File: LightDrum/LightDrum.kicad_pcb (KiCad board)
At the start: 4 copper layers, 108 x 83 mm, 221 parts, among them J102 JTAG, J1201 0525593652, J1203 PWR-CONN, J201 XLR3, J202 SJ-43515RS-SMT-TR, J601 LED D-SUB, J901 STD BARREL JACK, J902 STD BARREL JACK, K901 ALQ112, K902 ALQ112, Q101 RQ5A030AP, SW101 BOOT1, SW102 BOOT0, T701 NET-TIE, T702 NET-TIE, T703 NET-TIE, T704 NET-TIE, T705 NET-TIE, T706 NET-TIE, T707 NET-TIE, T708 NET-TIE, T709 NET-TIE, T710 NET-TIE, T711 NET-TIE, T712 NET-TIE, T713 NET-TIE, T714 NET-TIE, T715 NET-TIE, T716 NET-TIE, U1001 AP3401, U1002 LM22673-SOIC, U101 TCAN1044, U102 24LC04, U301 PCA9634_TSSOP20, U302 SQ2310ES_SOT23, U303 SQ2310ES_SOT23, U304 SQ2310ES_SOT23, U305 SQ2310ES_SOT23, U306 SQ2310ES_SOT23, U307 SQ2310ES_SOT23, U308 SQ2310ES_SOT23, U309 SQ2310ES_SOT23, U401 PCA9634_TSSOP20, U402 SQ2310ES_SOT23, U403 SQ2310ES_SOT23, U404 SQ2310ES_SOT23, U405 SQ2310ES_SOT23, U406 SQ2310ES_SOT23, U407 SQ2310ES_SOT23, U408 SQ2310ES_SOT23, U409 SQ2310ES_SOT23, U501 PCA9634_TSSOP20, U502 SQ2310ES_SOT23, U503 SQ2310ES_SOT23, U504 SQ2310ES_SOT23, U505 SQ2310ES_SOT23, U506 SQ2310ES_SOT23, U507 SQ2310ES_SOT23, U508 SQ2310ES_SOT23, U509 SQ2310ES_SOT23, U701 INA4181 A2, U702 INA4181 A2, U901 74HC2G08, U902 SSM3K361R_SOT23F, Y101 8MHz

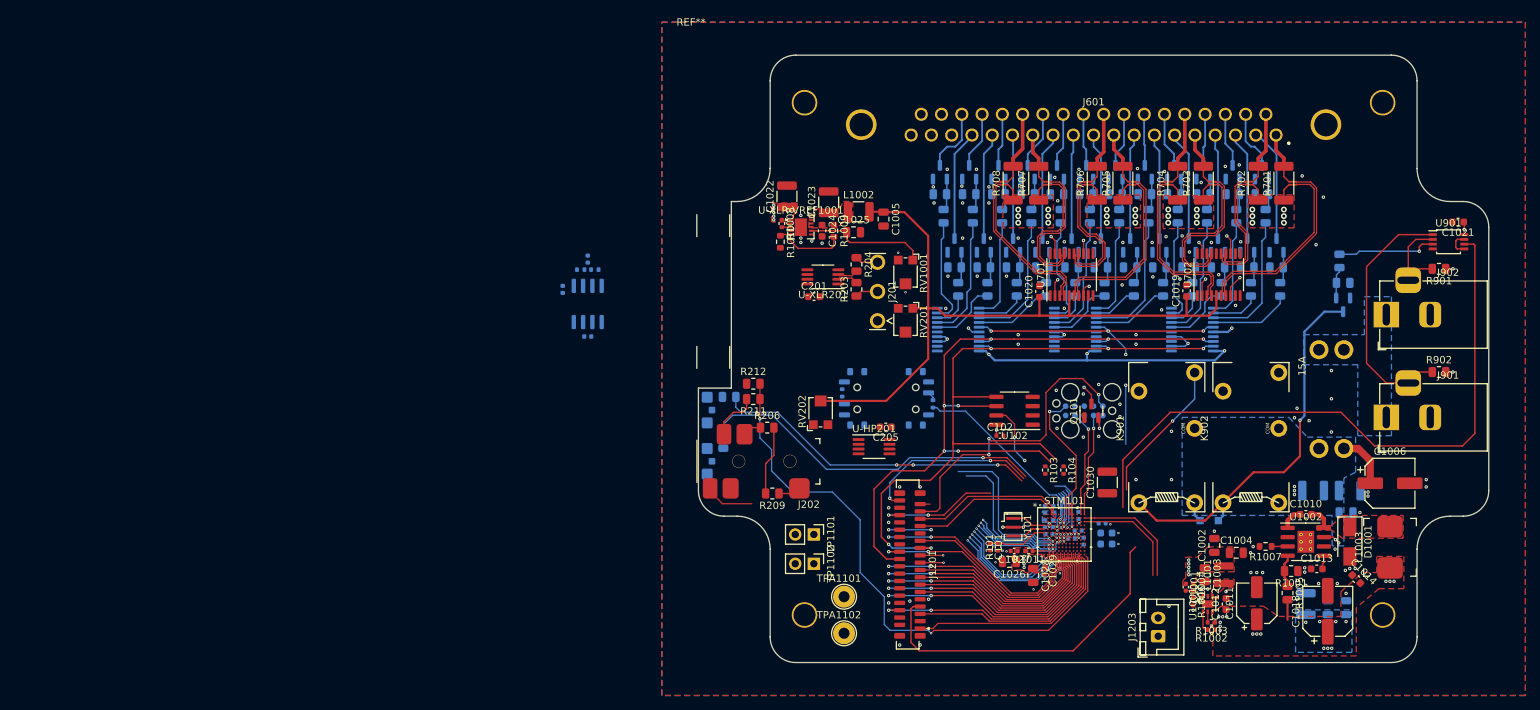
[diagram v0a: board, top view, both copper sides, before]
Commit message: Replace old MOSFETs with a more compact package
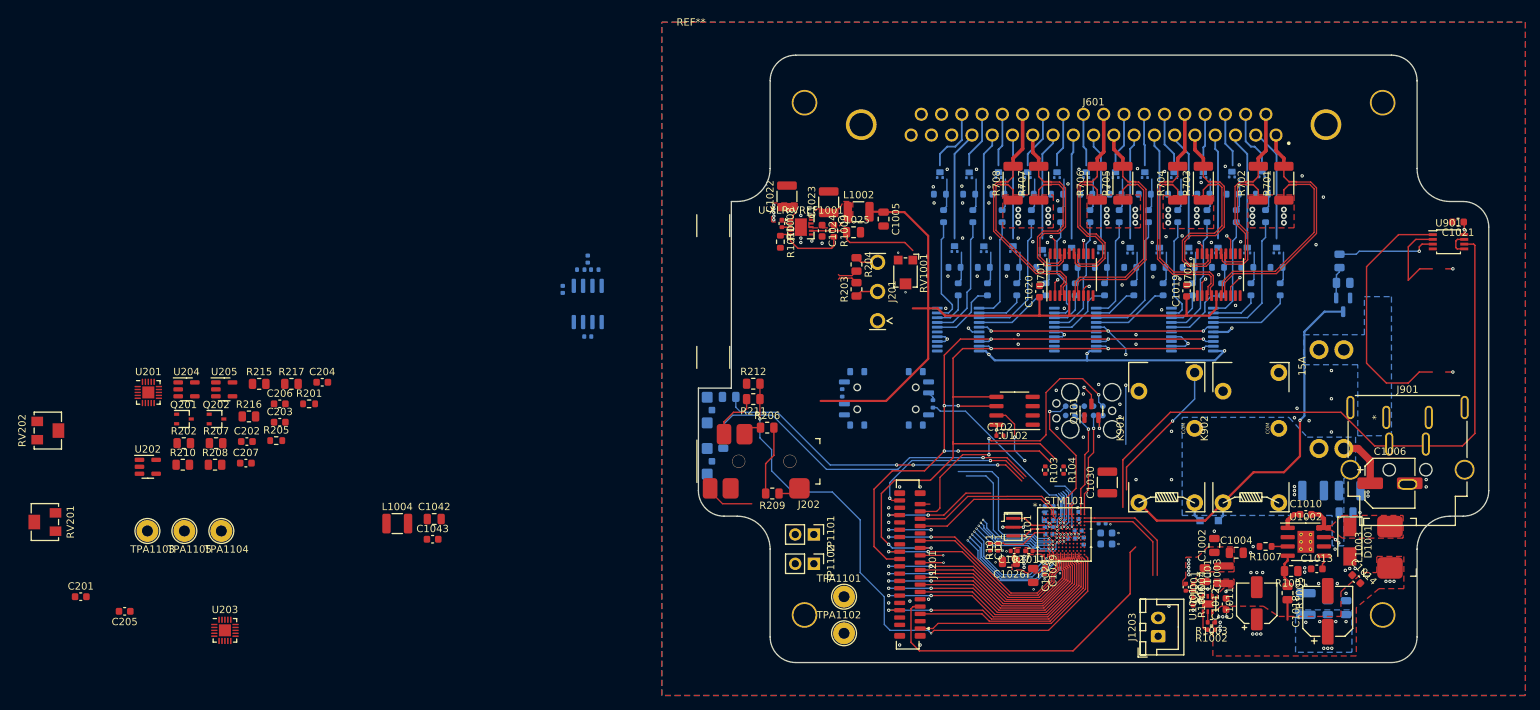
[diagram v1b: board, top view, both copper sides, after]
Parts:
- removed J902: STD BARREL JACK, Daxxn_Connectors:BarrelJack_Horizontal
- removed R901, R902: 10K, Resistor_SMD:R_0805_2012Metric
- removed U-HP201, U-XLR201: MCP3553-ESN, Package_SO:MSOP-8_3x3mm_P0.65mm
- removed U302, U303, U304, U305, U306, U307, U308, U309, U402, U403, U404, U405, U406, U407, U408, U409, U502, U503, U504, U505, U506, U507, U508, U509: SQ2310ES_SOT23, Package_TO_SOT_SMD:SOT-23
- added C1042: 1uF, Capacitor_SMD:C_0805_2012Metric, F.Cu at (-90.1, 21.9)
- added C1043: 100nF, Capacitor_SMD:C_0603_1608Metric, F.Cu at (-90.3, 24.6)
- added C202: 100nF, Capacitor_SMD:C_0603_1608Metric, F.Cu at (-115.7, 11.3)
- added C203: 100nF, Capacitor_SMD:C_0603_1608Metric, F.Cu at (-111.2, 8.66)
- added C204: 100nF, Capacitor_SMD:C_0603_1608Metric, F.Cu at (-105.4, 3.20)
- added C206: 100nF, Capacitor_SMD:C_0603_1608Metric, F.Cu at (-111.2, 6.15)
- added C207: 100nF, Capacitor_SMD:C_0603_1608Metric, F.Cu at (-115.8, 14.2)
- added L1004: 10uH, Capacitor_SMD:C_1210_3225Metric, F.Cu at (-95.2, 22.5)
- added Q201: NX6008NBKWX, Package_TO_SOT_SMD:SOT-323_SC-70, F.Cu at (-124.3, 8.22)
- added Q202: NX6008NBKWX, Package_TO_SOT_SMD:SOT-323_SC-70, F.Cu at (-119.8, 8.22)
- added Q301: PMXB43UNEZ, Daxxn_Packages:DFN1010D-3, B.Cu at (18.9, -25.3)
- added Q302: PMXB43UNEZ, Daxxn_Packages:DFN1010D-3, B.Cu at (21.0, -14.9)
- added Q303: PMXB43UNEZ, Daxxn_Packages:DFN1010D-3, B.Cu at (23.0, -25.3)
- added Q304: PMXB43UNEZ, Daxxn_Packages:DFN1010D-3, B.Cu at (25.0, -14.9)
- added Q305: PMXB43UNEZ, Daxxn_Packages:DFN1010D-3, B.Cu at (11.0, -25.2)
- added Q306: PMXB43UNEZ, Daxxn_Packages:DFN1010D-3, B.Cu at (13.0, -14.9)
- added Q307: PMXB43UNEZ, Daxxn_Packages:DFN1010D-3, B.Cu at (15.0, -25.2)
- added Q308: PMXB43UNEZ, Daxxn_Packages:DFN1010D-3, B.Cu at (17.0, -14.9)
- added Q401: PMXB43UNEZ, Daxxn_Packages:DFN1010D-3, B.Cu at (3.00, -25.2)
- added Q402: PMXB43UNEZ, Daxxn_Packages:DFN1010D-3, B.Cu at (5.00, -14.9)
- added Q403: PMXB43UNEZ, Daxxn_Packages:DFN1010D-3, B.Cu at (7.00, -25.2)
- added Q404: PMXB43UNEZ, Daxxn_Packages:DFN1010D-3, B.Cu at (9.00, -14.9)
- added Q405: PMXB43UNEZ, Daxxn_Packages:DFN1010D-3, B.Cu at (-5.00, -25.2)
- added Q406: PMXB43UNEZ, Daxxn_Packages:DFN1010D-3, B.Cu at (-3.00, -14.9)
- added Q407: PMXB43UNEZ, Daxxn_Packages:DFN1010D-3, B.Cu at (-1.00, -25.2)
- added Q408: PMXB43UNEZ, Daxxn_Packages:DFN1010D-3, B.Cu at (1.00, -14.9)
- added Q501: PMXB43UNEZ, Daxxn_Packages:DFN1010D-3, B.Cu at (-13.0, -25.2)
- added Q502: PMXB43UNEZ, Daxxn_Packages:DFN1010D-3, B.Cu at (-11.0, -15.1)
- added Q503: PMXB43UNEZ, Daxxn_Packages:DFN1010D-3, B.Cu at (-9.00, -25.2)
- added Q504: PMXB43UNEZ, Daxxn_Packages:DFN1010D-3, B.Cu at (-7.00, -14.6)
- added Q505: PMXB43UNEZ, Daxxn_Packages:DFN1010D-3, B.Cu at (-21.0, -25.2)
- added Q506: PMXB43UNEZ, Daxxn_Packages:DFN1010D-3, B.Cu at (-19.0, -15.1)
- added Q507: PMXB43UNEZ, Daxxn_Packages:DFN1010D-3, B.Cu at (-17.0, -25.2)
- added Q508: PMXB43UNEZ, Daxxn_Packages:DFN1010D-3, B.Cu at (-15.0, -15.1)
- added R201: 1K, Resistor_SMD:R_0603_1608Metric, F.Cu at (-107.2, 6.15)
- added R202: 10K, Resistor_SMD:R_0805_2012Metric, F.Cu at (-124.3, 11.5)
- added R205: 1K, Resistor_SMD:R_0603_1608Metric, F.Cu at (-111.7, 11.2)
- added R207: 10K, Resistor_SMD:R_0805_2012Metric, F.Cu at (-119.9, 11.5)
- added R208: 10K, Resistor_SMD:R_0805_2012Metric, F.Cu at (-120.0, 14.5)
- added R210: 1K, Resistor_SMD:R_0805_2012Metric, F.Cu at (-124.5, 14.5)
- added R215: 2.4K, Resistor_SMD:R_0805_2012Metric, F.Cu at (-114.0, 3.42)
- added R216: 7.5K, Resistor_SMD:R_0805_2012Metric, F.Cu at (-115.4, 7.87)
- added R217: 1K, Resistor_SMD:R_0805_2012Metric, F.Cu at (-109.6, 3.42)
- added TPA1103: VDD TP, TestPoint:TestPoint_Loop_D2.54mm_Drill1.5mm_Beaded, F.Cu at (-129.3, 23.5)
- added TPA1104: VDDA TP, TestPoint:TestPoint_Loop_D2.54mm_Drill1.5mm_Beaded, F.Cu at (-119.2, 23.5)
- added TPA1105: VREF TP, TestPoint:TestPoint_Loop_D2.54mm_Drill1.5mm_Beaded, F.Cu at (-124.2, 23.5)
- added U201: MCP3561R, Package_DFN_QFN:QFN-20-1EP_3x3mm_P0.4mm_EP1.65x1.65mm, F.Cu at (-129.2, 4.59)
- added U202: AZV321, Package_TO_SOT_SMD:SOT-23-5, F.Cu at (-129.2, 14.8)
- added U203: MCP3561R, Package_DFN_QFN:QFN-20-1EP_3x3mm_P0.4mm_EP1.65x1.65mm, F.Cu at (-118.7, 37.1)
- added U204: AZV321, Package_TO_SOT_SMD:SOT-23-5, F.Cu at (-124.0, 4.17)
- added U205: AZV321, Package_TO_SOT_SMD:SOT-23-5, F.Cu at (-118.8, 4.17)
- J901: value STD BARREL JACK -> DIN-4-SH; footprint Daxxn_Connectors:BarrelJack_Horizontal -> Daxxn_Connectors:KPJXHT-4S-S
- R106, R107: value 10K -> 60
- R213, R214: value 330 -> 1K
- R301, R302, R303, R304, R305, R306, R307, R308, R309, R310, R311, R312, R313, R314, R315, R316, R401, R402, R403, R404, R405, R406, R407, R408, R409, R410, R411, R412, R413, R414, R415, R416, R501, R502, R503, R504, R505, R506, R507, R508, R509, R510, R511, R512, R513, R514, R515, R516: footprint Resistor_SMD:R_0805_2012Metric -> Resistor_SMD:R_0603_1608Metric
- RV201, RV202: footprint Daxxn_Switches:Bourns_TC33X -> Potentiometer_SMD:Potentiometer_Bourns_3214W_Vertical
- moved RV201 120.7 mm to (-143.3, 22.3)
- moved C201 108.3 mm to (-138.4, 32.5)
- moved C205 107.0 mm to (-132.4, 34.5)
- moved RV202 105.6 mm to (-142.9, 9.80)
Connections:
- net /HP-SW renamed /Audio Inputs/HP-SW-IN
- net CANH renamed CAN+
- net CANL renamed CAN-
- C1002 pad 2: GND -> AGND
- C1003 pad 2: GND -> AGND
- C1004 pad 2: GND -> AGND
- C1005 pad 1: VDDA -> Net-(C1023-Pad1)
- C1005 pad 2: GND -> AGND
- C1006 pad 2: GND -> AGND
- C1007 pad 1: GND -> AGND
- C1008 pad 1: GND -> AGND
- C1009 pad 1: GND -> AGND
- C101 pad 2: GND -> AGND
- C1011 pad 2: GND -> AGND
- C1012 pad 2: GND -> AGND
- C1013 pad 1: GND -> AGND
- C1014 pad 1: GND -> AGND
- C1015 pad 1: GND -> AGND
- C1016 pad 1: GND -> AGND
- C1017 pad 1: GND -> AGND
- C1018 pad 2: GND -> AGND
- C1019 pad 2: GND -> AGND
- C102 pad 2: GND -> AGND
- C1020 pad 2: GND -> AGND
- C1021 pad 2: GND -> AGND
- C1022 pad 2: GND -> AGND
- C1023 pad 2: GND -> AGND
- C1024 pad 1: Net-(C1023-Pad1) -> Net-(C1024-Pad1)
- C1024 pad 2: GND -> AGND
- C1025 pad 2: GND -> AGND
- C1026 pad 2: GND -> AGND
- C1027 pad 2: GND -> AGND
- C1028 pad 2: GND -> AGND
- C1029 pad 2: GND -> AGND
- C103 pad 2: GND -> AGND
- C1030 pad 2: GND -> AGND
- C1031 pad 2: GND -> AGND
- C1032 pad 2: GND -> AGND
- C1033 pad 2: GND -> AGND
- C1034 pad 2: GND -> AGND
- C1035 pad 2: GND -> AGND
- C1036 pad 2: GND -> AGND
- C1037 pad 2: GND -> AGND
- C1038 pad 2: GND -> AGND
- C1039 pad 2: GND -> AGND
- C104 pad 2: GND -> AGND
- C1040 pad 2: GND -> AGND
- C1041 pad 2: GND -> AGND
- C105 pad 1: GND -> AGND
- C106 pad 1: GND -> AGND
- C107 pad 1: GND -> AGND
- C201 pad 1: VDD -> VDDA
- C201 pad 2: GND -> AGND
- C205 pad 2: GND -> AGND
- D1001 pad 2: GND -> AGND
- D201 pad 1: GND -> Net-(R213-Pad2)
- D201 pad 2: Net-(D201-Pad2) -> VCC
- D202 pad 1: GND -> Net-(D202-Pad1)
- D202 pad 2: Net-(D202-Pad2) -> VCC
- J102 pad 3: GND -> AGND
- J102 pad 5: GND -> AGND
- J102 pad 9: GND -> AGND
- J1201 pad 3: GND -> AGND
- J1201 pad 30: GND -> AGND
- J1201 pad 34: GND -> AGND
- J1201 pad 8: GND -> AGND
- J1201 pad 9: GND -> AGND
- J1201 pad M: GND -> AGND
- J1203 pad 2: GND -> AGND
- J201 pad 1: GND -> AGND
- J601 pad 0: GND -> AGND
- J601 pad 19: GND -> AGND
- J901 pad 2: GND -> Net-(F901-Pad1)
- J901 pad 3: Net-(J901-Pad3) -> AGND
- L1002 pad 2: VDDA -> Net-(C1024-Pad1)
- Q101 pad 1: GND -> AGND
- R1001 pad 1: GND -> AGND
- R1006 pad 2: GND -> AGND
- R1007 pad 2: GND -> AGND
- R1010 pad 2: GND -> AGND
- R212 pad 1: GND -> AGND
- R213 pad 1: /HP-SEL-IND -> Net-(R213-Pad1)
- R213 pad 2: Net-(D201-Pad2) -> Net-(R213-Pad2)
- R214 pad 1: /XLR-SEL-IND -> Net-(R214-Pad1)
- R214 pad 2: Net-(D202-Pad2) -> Net-(D202-Pad1)
- R305 pad 2: GND -> AGND
- R306 pad 2: GND -> AGND
- R307 pad 2: GND -> AGND
- R308 pad 2: GND -> AGND
- R313 pad 2: GND -> AGND
- R314 pad 2: GND -> AGND
- R315 pad 2: GND -> AGND
- R316 pad 2: GND -> AGND
- R405 pad 2: GND -> AGND
- R406 pad 2: GND -> AGND
- R407 pad 2: GND -> AGND
- R408 pad 2: GND -> AGND
- R413 pad 2: GND -> AGND
- R414 pad 2: GND -> AGND
- R415 pad 2: GND -> AGND
- R416 pad 2: GND -> AGND
- R505 pad 2: GND -> AGND
- R506 pad 2: GND -> AGND
- R507 pad 2: GND -> AGND
- R508 pad 2: GND -> AGND
- R513 pad 2: GND -> AGND
- R514 pad 2: GND -> AGND
- R515 pad 2: GND -> AGND
- R516 pad 2: GND -> AGND
- R903 pad 1: Net-(R903-Pad1) -> /STRIP-PWR
- R904 pad 2: GND -> AGND
- RV1001 pad 2: GND -> AGND
- RV1001 pad 3: GND -> AGND
- RV201 pad 1: VDDA -> AGND
- RV201 pad 2: VDDA -> AGND
- RV202 pad 1: VDDA -> Net-(RV202-Pad1)
- RV202 pad 2: VDDA -> AGND
- RV202 pad 3: Net-(RV202-Pad3) -> AGND
- STM101 pad D2: GND -> AGND
- STM101 pad E6: GND -> AGND
- STM101 pad E7: GND -> AGND
- STM101 pad G10: GND -> AGND
- STM101 pad G4: GND -> AGND
- STM101 pad G8: GND -> AGND
- STM101 pad H5: GND -> AGND
- STM101 pad H6: GND -> AGND
- STM101 pad J1: GND -> AGND
- STM101 pad K1: GND -> AGND
- SW101 pad 3: GND -> AGND
- SW102 pad 3: GND -> AGND
- TPA1102 pad 1: GND -> AGND
- U-XLR-VREF1001 pad 11: GND -> AGND
- U-XLR-VREF1001 pad 6: GND -> AGND
- U1001 pad 5: GND -> AGND
- U1001 pad 7: GND -> AGND
- U1002 pad 6: GND -> AGND
- U1002 pad 9: GND -> AGND
- U101 pad 2: GND -> AGND
- U102 pad 1: GND -> AGND
- U102 pad 2: GND -> AGND
- U102 pad 3: GND -> AGND
- U102 pad 4: GND -> AGND
- U301 pad 1: GND -> AGND
- U301 pad 10: GND -> AGND
- U301 pad 17: GND -> AGND
- U301 pad 3: GND -> AGND
- U301 pad 5: GND -> AGND
- U401 pad 1: GND -> AGND
- U401 pad 10: GND -> AGND
- U401 pad 16: GND -> AGND
- U401 pad 17: GND -> AGND
- U401 pad 2: GND -> AGND
- U401 pad 3: GND -> AGND
- U501 pad 1: GND -> AGND
- U501 pad 10: GND -> AGND
- U501 pad 17: GND -> AGND
- U501 pad 2: GND -> AGND
- U501 pad 5: GND -> AGND
- U701 pad 1: GND -> AGND
- U701 pad 12: GND -> AGND
- U701 pad 16: GND -> AGND
- U701 pad 20: GND -> AGND
- U701 pad 9: GND -> AGND
- U702 pad 1: GND -> AGND
- U702 pad 12: GND -> AGND
- U702 pad 16: GND -> AGND
- U702 pad 20: GND -> AGND
- U702 pad 9: GND -> AGND
- U901 pad 1: Net-(J901-Pad3) -> (no net)
- U901 pad 2: Net-(J902-Pad3) -> (no net)
- U901 pad 3: Net-(R903-Pad1) -> (no net)
- U901 pad 4: GND -> AGND
- U901 pad 5: Net-(U901-Pad5) -> (no net)
- U901 pad 6: /STRIP-PWR -> (no net)
- U901 pad 7: Net-(U901-Pad5) -> (no net)
- U902 pad 2: GND -> AGND
- Y101 pad 2: GND -> AGND
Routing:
- net AGND: track 0.00 -> 92.3 mm, vias 0 -> 132
- net /STRIP-PWR: track 133.5 -> 60.0 mm, vias 0 -> 1
- net (no net): track 0.00 -> 50.5 mm
- net Net-(R213-Pad1): track 0.00 -> 48.1 mm, vias 0 -> 1
- net /HP-SEL-IND: track 48.1 -> 0.00 mm, vias 1 -> 0
- net Net-(R214-Pad1): track 0.00 -> 44.7 mm, vias 0 -> 3
- net /XLR-SEL-IND: track 44.7 -> 0.00 mm, vias 3 -> 0
- net Net-(J901-Pad3): track 34.8 -> 0.00 mm
- net Net-(R903-Pad1): track 13.7 -> 0.00 mm, vias 1 -> 0
- net Net-(J902-Pad3): track 12.3 -> 0.00 mm
- net GND: track 5.25 -> 0.00 mm, vias 132 -> 0
- net Net-(U901-Pad5): track 3.37 -> 0.00 mm
- net Net-(C1025-Pad1): track 16.8 -> 15.5 mm
- added copper zone on B.Cu, net AGND
- added copper zone on F.Cu, net AGND
- added copper zone on In1.Cu, net AGND
- removed copper zone on B.Cu, net GND
- removed copper zone on F.Cu, net GND
- removed copper zone on In1.Cu, net GND
